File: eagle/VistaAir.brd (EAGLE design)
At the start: 100 x 80 mm, 6 parts

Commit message: pcb corrections
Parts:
- added J3: (no value), SparkFun-Connectors:1X04
- B2: device SparkFun-Boards:ESP32_THING -> kevins_parts:ESP32_THING
- moved J1 6.02 mm to (29.2, 12.7)
- moved J2 3.97 mm to (47.8, 53.3)
- moved U$1 3.57 mm to (14.2, 12.7)
- moved U$2 2.05 mm to (44.5, 12.7)
- moved B2 1.85 mm to (16.5, 27.7)
- moved B1 0.76 mm to (26.7, 33.8), flipped to the bottom, turned to 180 degrees
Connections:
- removed net GND_OUT: U$1.GND_OUT, U$2.GND_OUT
- removed net LOGIC_V: B2.36
- new net CWL2: B2.7
- new net NC1: B2.35
- new net NC2: B2.34
- net 3V6: now also J3.2; no longer B1.5V
- net BOARD_GND: now also B1.GND@0, B2.1, J3.1, U$1.GND_OUT, U$2.GND_OUT; no longer B1.3.3V, B1.RES, B2.37
- net CCL1: now also B1.D8, B2.11; no longer B1.SDA, B2.8
- net CCL2: now also B1.D9, B2.12; no longer B1.SCL, B2.7
- net CLW1: now also B1.D7, B2.10; no longer B1.D10, B2.12
- net CLW2: now also B1.D4; no longer B1.D13, B2.9
- net ENC1A: now also B2.28; no longer B2.33
- net ENC1B: now also B2.27; no longer B2.32
- net ENC2A: now also B2.33, J3.3; no longer B1.GND@0, B2.35
- net ENC2B: now also B2.32, J3.4; no longer B1.GND@1, B2.34
- net LED: now also B2.22; no longer B2.27
- net LIMBOTA: now also B2.24; no longer B2.29
- net LIMBOTB: now also B2.23; no longer B2.28
- net LIMTOPA: now also B2.26; no longer B2.31
- net LIMTOPB: now also B2.25; no longer B2.30
- net PWM1: now also B1.D5, B2.8; no longer B1.D12, B2.10
- net PWM2: now also B1.D6, B2.9; no longer B1.D11, B2.11
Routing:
- net BOARD_GND: track 100.0 -> 180.0 mm
- net V5IN: track 10.9 -> 52.0 mm
- net GND_OUT: track 30.4 -> 0.00 mm
- net CLW2: track 29.5 -> 0.00 mm
- net GND12: track 33.2 -> 45.2 mm
- net 3V6: track 56.7 -> 47.8 mm
- net V12: track 33.8 -> 42.1 mm
- net ENC1B: track 15.3 -> 7.76 mm
- net ENC1A: track 15.3 -> 7.76 mm
- net LIMTOPB: track 15.3 -> 7.76 mm
- net LIMBOTB: track 15.3 -> 7.76 mm
- net LIMTOPA: track 15.3 -> 7.76 mm
- net LED: track 15.3 -> 7.76 mm
- net LIMBOTA: track 15.3 -> 7.76 mm
- net ENC2B: track 12.5 -> 7.89 mm
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- added copper zone on layer 1, net N$1
- removed copper zone on layer 1, net GND

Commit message: beta 1 board corrections
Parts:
- moved U$1 1.64 mm to (15.8, 12.5)
- moved J1 1.25 mm to (30.5, 12.8)
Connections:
- removed net CWL2: B2.7
- net CLW2: now also B2.7
- net V5IN: now also B1.5V; no longer B1.VIN
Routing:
- net 3V6: track 47.8 -> 106.9 mm
- net CCL2: track 31.6 -> 81.6 mm
- net CLW2: track 0.00 -> 32.0 mm
- net BOARD_GND: track 180.0 -> 159.8 mm
- net GND12: track 45.2 -> 34.3 mm
- net V12: track 42.1 -> 51.8 mm
- net V5IN: track 52.0 -> 49.7 mm
- net PWM2: track 32.8 -> 32.0 mm
- net PWM1: track 32.8 -> 32.0 mm
- net CCL1: track 31.6 -> 30.8 mm
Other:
- board size 100 x 80 mm -> 58.6 x 91.2 mm

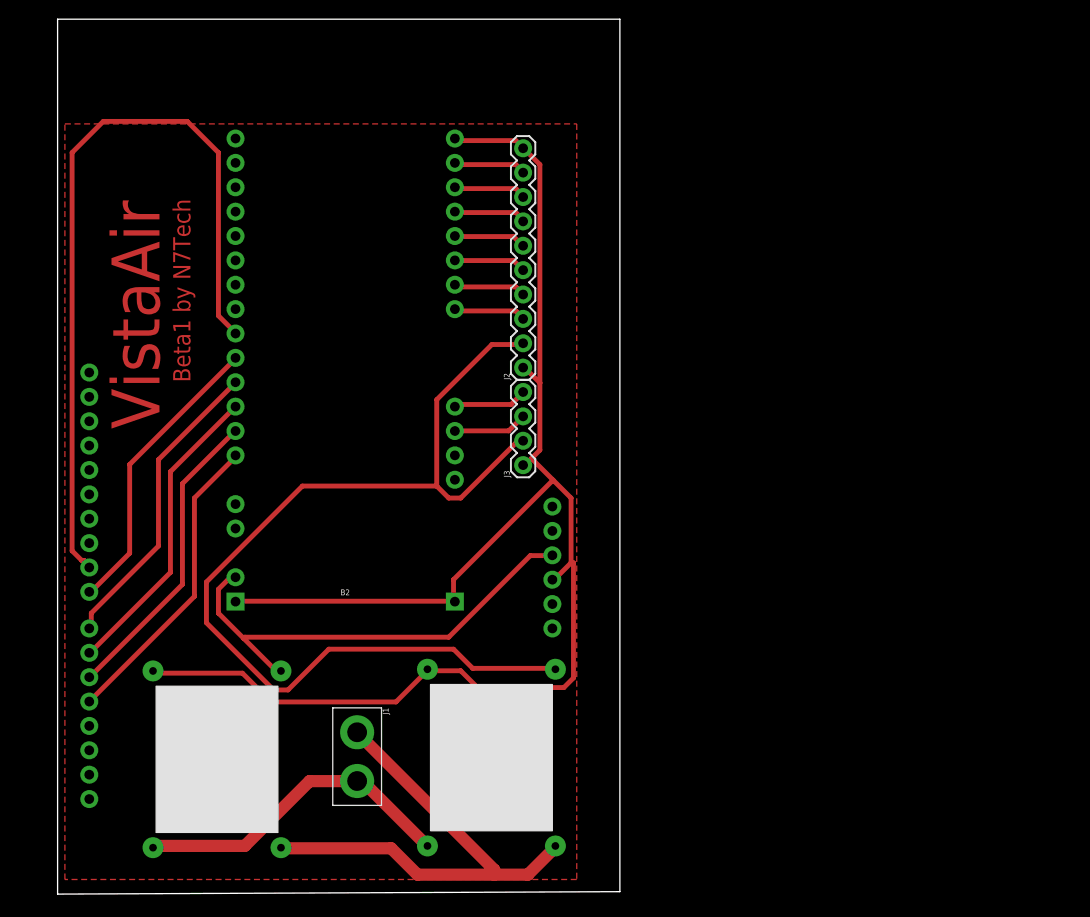
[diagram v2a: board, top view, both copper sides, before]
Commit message: updated board for stable power - which I believe was showstopper
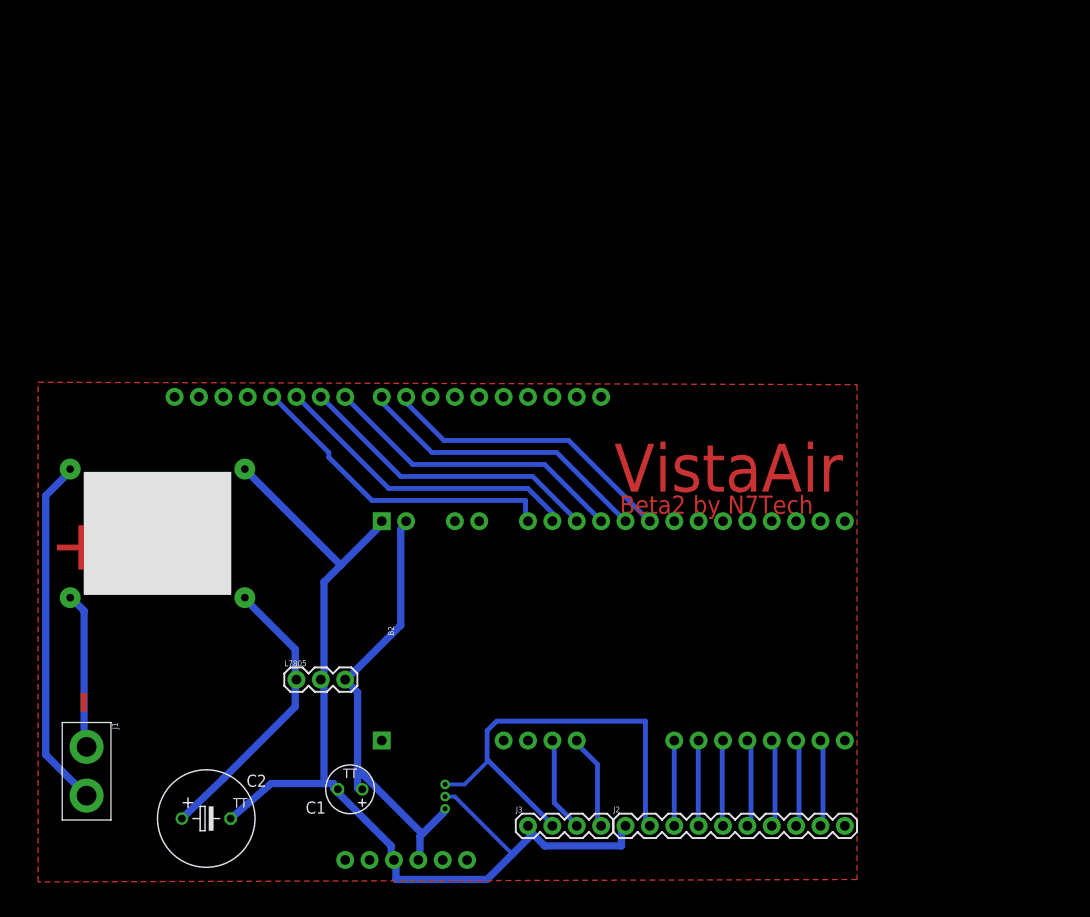
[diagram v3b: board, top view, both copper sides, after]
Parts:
- added C1: 10mu, adafruit:TT2D5
- added C2: 330mu, adafruit:TT5D10
- added L7805: (no value), SparkFun-Connectors:1X03
- U$1: value MP1584EN_STEPDOWN_MODULE -> MCP1702_LDOREGULATOR; device kevins_parts:MP1584EN_STEPDOWN_MODULE -> kevins_parts:MCP1702_LDOREGULATOR
- moved J2 48.9 mm to (58.4, 5.59), turned to 0 degrees
- moved U$2 41.9 mm to (9.65, 36.1), turned to 0 degrees
- moved J3 37.6 mm to (48.3, 5.59), turned to 0 degrees
- moved J1 28.2 mm to (2.26, 11.3)
- moved U$1 23.8 mm to (38.4, 4.83), turned to 0 degrees
- moved B2 18.7 mm to (31.8, 38.6), turned to 270 degrees
- moved B1 12.7 mm to (36.8, 26.2), turned to 270 degrees
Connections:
- new net 5V5: C2.+, L7805.1, U$2.VOUT
- net 3V6: now also U$1.P$1; no longer U$2.VOUT
- net BOARD_GND: now also C1.-, C2.-, L7805.2, U$1.P$2; no longer B2.21, B2.40, J2.10, U$1.GND_OUT
- net GND12: no longer U$1.GND_IN
- net V12: no longer U$1.VIN
- net V5IN: now also C1.+, L7805.3, U$1.P$3; no longer U$1.VOUT
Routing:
- net 3V6: track 106.9 -> 46.3 mm
- net BOARD_GND: track 159.8 -> 108.3 mm
- net CCL2: track 81.6 -> 31.2 mm
- net V12: track 51.8 -> 16.3 mm
- net 5V5: track 0.00 -> 30.2 mm
- net GND12: track 34.3 -> 36.8 mm
- net V5IN: track 49.7 -> 47.5 mm
- net ENC2A: track 7.74 -> 9.88 mm
- net ENC2B: track 7.82 -> 9.89 mm
- net LIMTOPB: track 7.58 -> 9.17 mm
- net CLW2: track 32.0 -> 33.5 mm
- net LIMBOTA: track 7.63 -> 9.12 mm
- net LIMBOTB: track 7.62 -> 9.07 mm
- net LED: track 7.61 -> 9.03 mm
- net LIMTOPA: track 7.53 -> 8.90 mm
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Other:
- board outline removed
- board text added: "+"
- board text added: "-"
- board text added: "Beta2 by N7Tech"
- board text removed: "Beta1 by N7Tech"

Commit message: proper stable power supply on board with buck converter into liner regulators
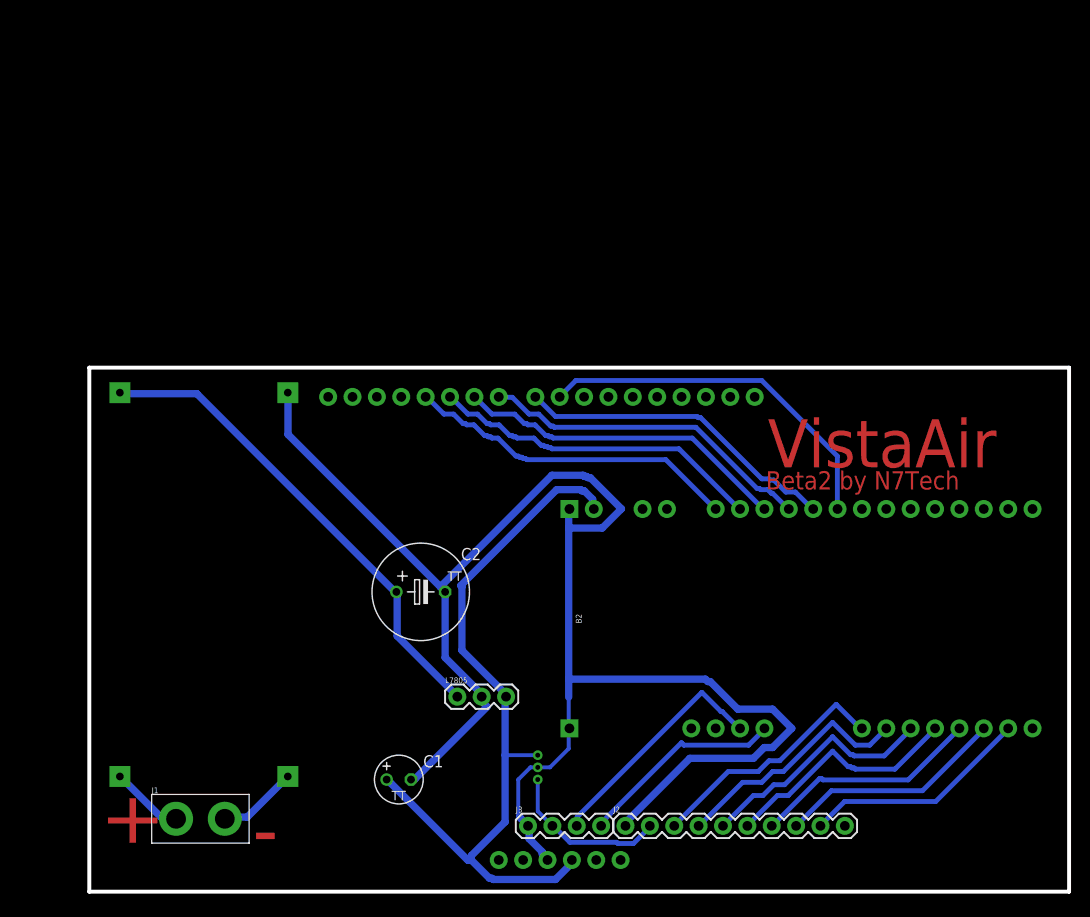
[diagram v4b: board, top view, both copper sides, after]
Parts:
- U$2: value MP1584EN_STEPDOWN_MODULE -> LM2596_STEPDOWN_MODULE; device kevins_parts:MP1584EN_STEPDOWN_MODULE -> kevins_parts:LM2596_STEPDOWN_MODULE
- moved C2 32.5 mm to (37.1, 30.0)
- moved B2 19.6 mm to (51.3, 39.9)
- moved L7805 16.9 mm to (40.9, 19.1)
- moved U$1 16.2 mm to (50.5, 15.5), turned to 180 degrees
- moved B1 16.0 mm to (52.8, 26.2)
- moved J1 12.9 mm to (14.1, 6.32), turned to 0 degrees
- moved U$2 7.19 mm to (14.5, 30.7), turned to 270 degrees
- moved C1 5.18 mm to (34.8, 10.4), turned to 0 degrees
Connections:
- net BOARD_GND: now also U$2.GNDOUT; no longer U$2.GND_OUT
- net GND12: now also U$2.GNDIN; no longer U$2.GND_IN
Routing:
- net BOARD_GND: track 108.3 -> 172.9 mm
- net V5IN: track 47.5 -> 79.6 mm
- net 3V6: track 46.3 -> 17.7 mm
- net GND12: track 36.8 -> 8.51 mm
- net 5V5: track 30.2 -> 51.0 mm
- net ENC1A: track 8.89 -> 26.0 mm
- net ENC1B: track 8.89 -> 25.7 mm
- net LIMTOPA: track 8.90 -> 25.5 mm
- net LIMTOPB: track 9.17 -> 25.4 mm
- net ENC2A: track 9.88 -> 24.8 mm
- net LED: track 9.03 -> 23.8 mm
- net LIMBOTB: track 9.07 -> 23.8 mm
- net LIMBOTA: track 9.12 -> 23.9 mm
- net ENC2B: track 9.89 -> 21.7 mm
- net V12: track 16.3 -> 7.71 mm
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- removed copper zone on layer 1, net N$1
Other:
- board outline added: 102.1 x 54.6 mm

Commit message: update board with logic converer from 3.3v esp32 to 5v monster moto board
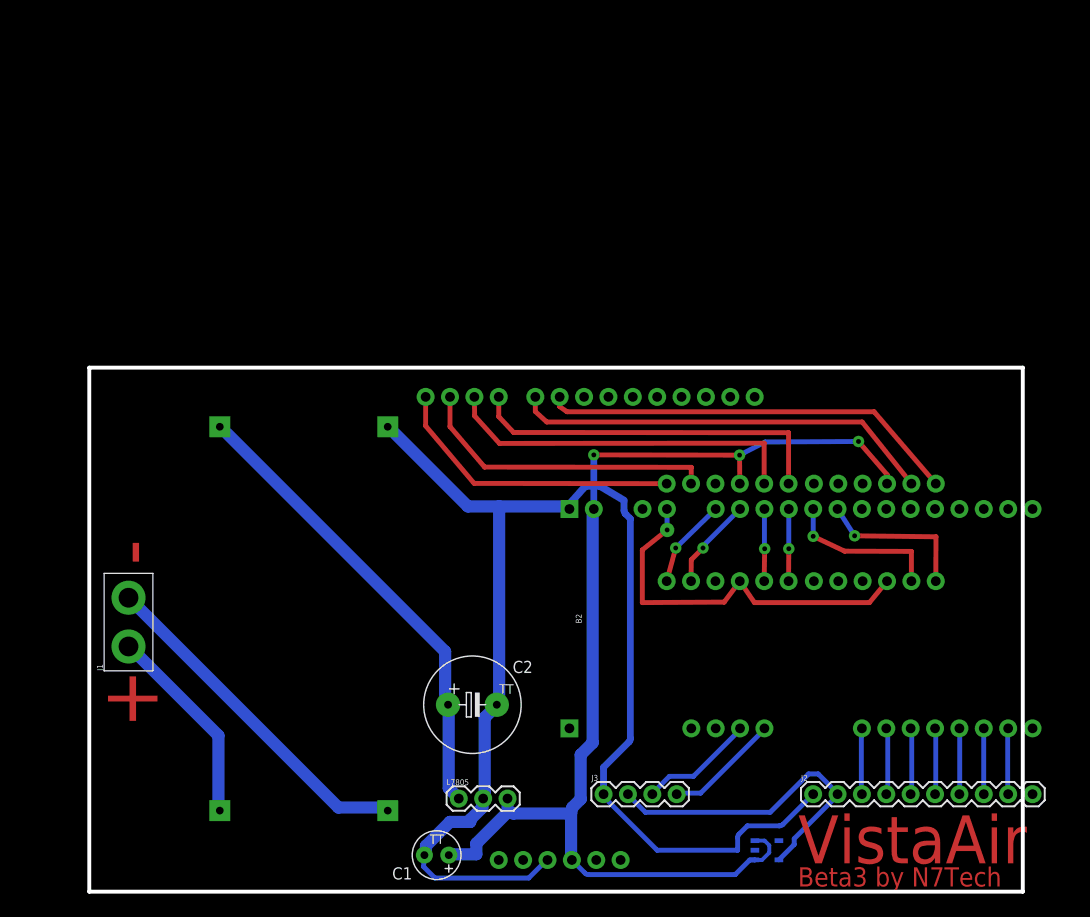
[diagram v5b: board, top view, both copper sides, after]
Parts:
- added B3, B4: SPARKFUN_LOGIC_LEVEL_CONVERTER, SparkFun-Boards:SPARKFUN_LOGIC_LEVEL_CONVERTER
- U$1: value MCP1702_LDOREGULATOR -> LDO_REGULATOR_LP2985-N; device kevins_parts:MCP1702_LDOREGULATOR -> kevins_parts:LDO_REGULATOR_LP2985-N
- moved U$1 26.0 mm to (73.4, 3.05), flipped to the bottom
- moved J1 21.8 mm to (6.63, 26.8), turned to 90 degrees
- moved J2 19.8 mm to (78.0, 8.89)
- moved C2 12.9 mm to (42.5, 18.2)
- moved U$2 11.0 mm to (24.9, 27.2)
- moved L7805 10.6 mm to (41.0, 8.43)
- moved C1 8.80 mm to (38.7, 2.54), turned to 180 degrees
- moved J3 8.54 mm to (56.1, 8.89)
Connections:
- removed net CCL1: B1.D8, B2.11
- removed net CCL2: B1.D9, B2.12
- removed net CLW1: B1.D7, B2.10
- removed net CLW2: B1.D4, B2.7
- removed net PWM1: B1.D5, B2.8
- removed net PWM2: B1.D6, B2.9
- new net 3V3: B2.5, B3.LV, B4.LV
- new net CCL1_3V3: B2.11, B4.LV2
- new net CCL1_5V: B1.D8, B4.HV2
- new net CCL2_3V3: B2.12, B4.LV1
- new net CCL2_5V: B1.D9, B4.HV1
- new net CLW1_3V3: B2.10, B3.LV1
- new net CLW1_5V: B1.D7, B3.HV1
- new net CLW2_3V3: B2.7, B3.LV4
- new net CLW2_5V: B1.D4, B3.HV4
- new net N$1: B3.GND1
- new net N$2: B3.GND2
- new net N$3: B4.GND1
- new net N$4: B4.GND2
- new net NC: U$1.BYPASS
- new net PWM1_3V3: B2.8, B3.LV3
- new net PWM1_5V: B1.D5, B3.HV3
- new net PWM2_3V3: B2.9, B3.LV2
- new net PWM2_5V: B1.D6, B3.HV2
- net 3V6: now also U$1.VOUT; no longer U$1.P$1
- net BOARD_GND: now also U$1.GND; no longer U$1.P$2
- net V5IN: now also B3.HV, B4.HV, U$1.CNTRL, U$1.VIN; no longer U$1.P$3
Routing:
- net CCL1_5V: track 0.00 -> 44.2 mm
- net CCL2_5V: track 0.00 -> 43.8 mm
- net V5IN: track 79.6 -> 120.3 mm, vias 0 -> 3
- net 3V3: track 0.00 -> 39.8 mm, vias 0 -> 1
- net CCL2: track 38.4 -> 0.00 mm
- net CLW1_5V: track 0.00 -> 38.3 mm
- net PWM2_5V: track 0.00 -> 37.6 mm
- net PWM2: track 35.2 -> 0.00 mm
- net CLW2: track 35.1 -> 0.00 mm
- net CLW1: track 35.1 -> 0.00 mm
- net PWM1: track 35.0 -> 0.00 mm
- net CCL1: track 33.8 -> 0.00 mm
- net PWM1_5V: track 0.00 -> 31.9 mm
- net CLW2_5V: track 0.00 -> 30.9 mm
- net GND12: track 8.51 -> 36.3 mm
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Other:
- board size 102.1 x 54.6 mm -> 97.3 x 54.6 mm
- board text added: "Beta3 by N7Tech"
- board text removed: "Beta2 by N7Tech"
